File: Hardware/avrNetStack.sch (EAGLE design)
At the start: 36 parts, among them IC1 MEGA48/88/168-PU, IC2 ENC28J60SP, Q1 16M, Q2 25M

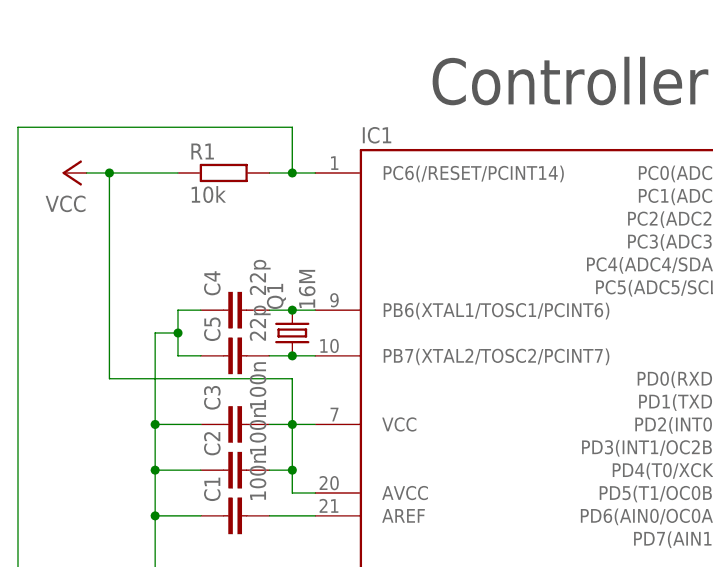
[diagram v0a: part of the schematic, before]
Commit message: AVR runs with 20MHz
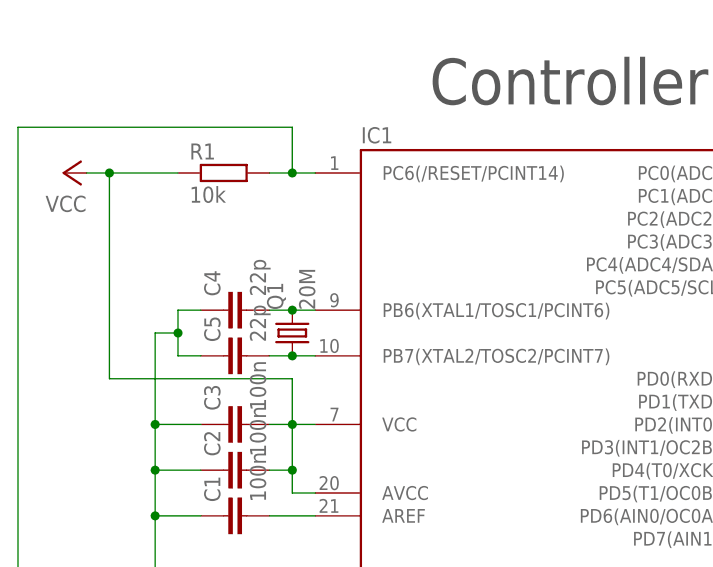
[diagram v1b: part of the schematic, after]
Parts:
- Q1: value 16M -> 20M
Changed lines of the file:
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@@
 <part name="C4" library="resistor" deviceset="C-EU" device="025-030X050" value="22p"/>
 <part name="C5" library="resistor" deviceset="C-EU" device="025-030X050" value="22p"/>
-<part name="Q1" library="crystal" deviceset="CRYSTAL" device="HC49S" value="16M"/>
+<part name="Q1" library="crystal" deviceset="CRYSTAL" device="HC49S" value="20M"/>
 <part name="JP1" library="0_RN" deviceset="AVR-ISP" device=""/>
 <part name="GND2" library="supply1" deviceset="GND" device=""/>

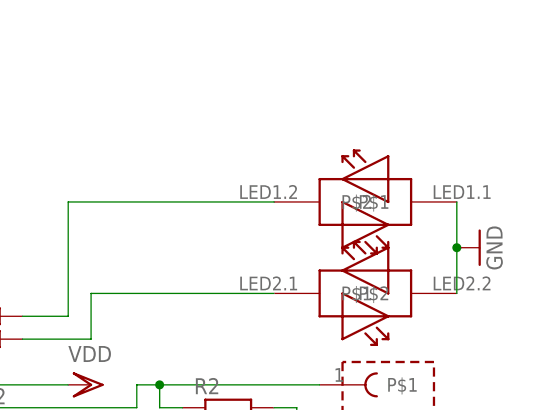
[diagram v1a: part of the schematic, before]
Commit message: Added PHY Initialization for ENC
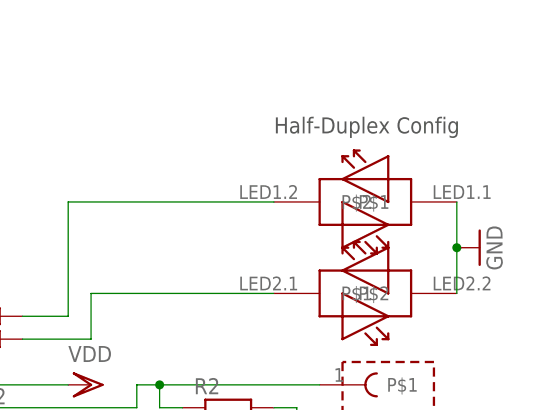
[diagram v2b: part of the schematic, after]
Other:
- note added: "Half-Duplex Config"
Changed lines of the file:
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@@
 <text x="177.8" y="109.22" size="1.27" layer="97">AVR Input is 3V3 tolerant</text>
 <text x="175.26" y="111.76" size="1.27" layer="97">ENC &amp; MRF Input is 5V5 Tolerant</text>
+<text x="332.74" y="109.22" size="1.778" layer="97">Half-Duplex Config</text>
 </plain>
 <instances>

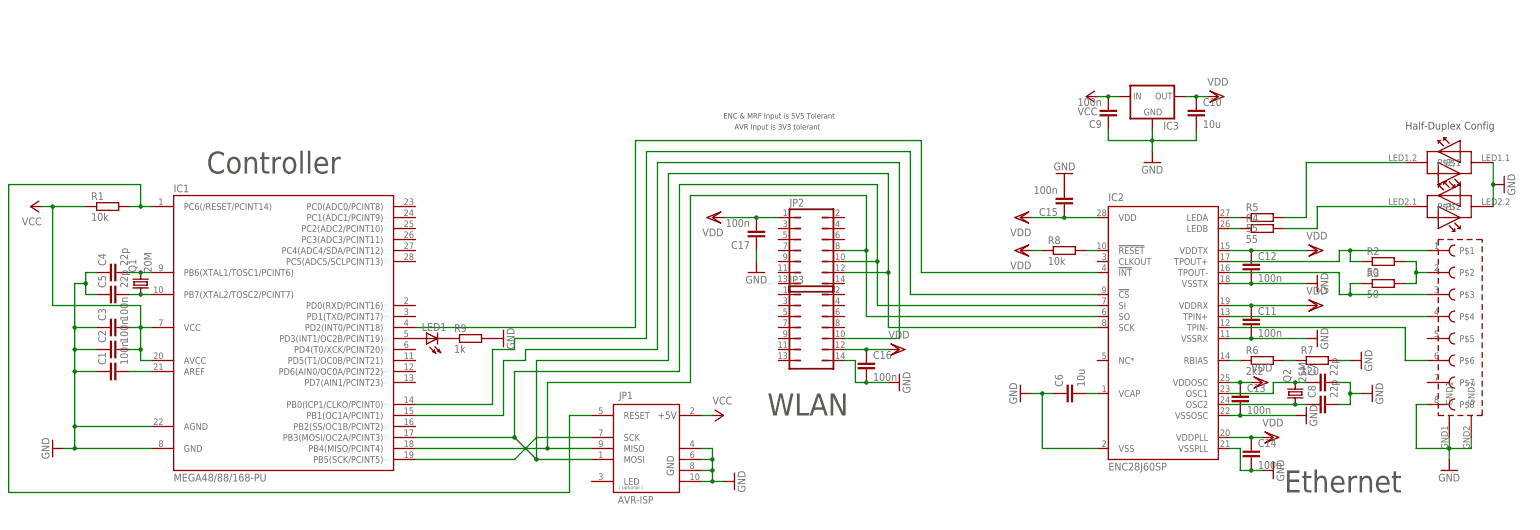
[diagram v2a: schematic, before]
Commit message: Changed Schematic for AtMega32.
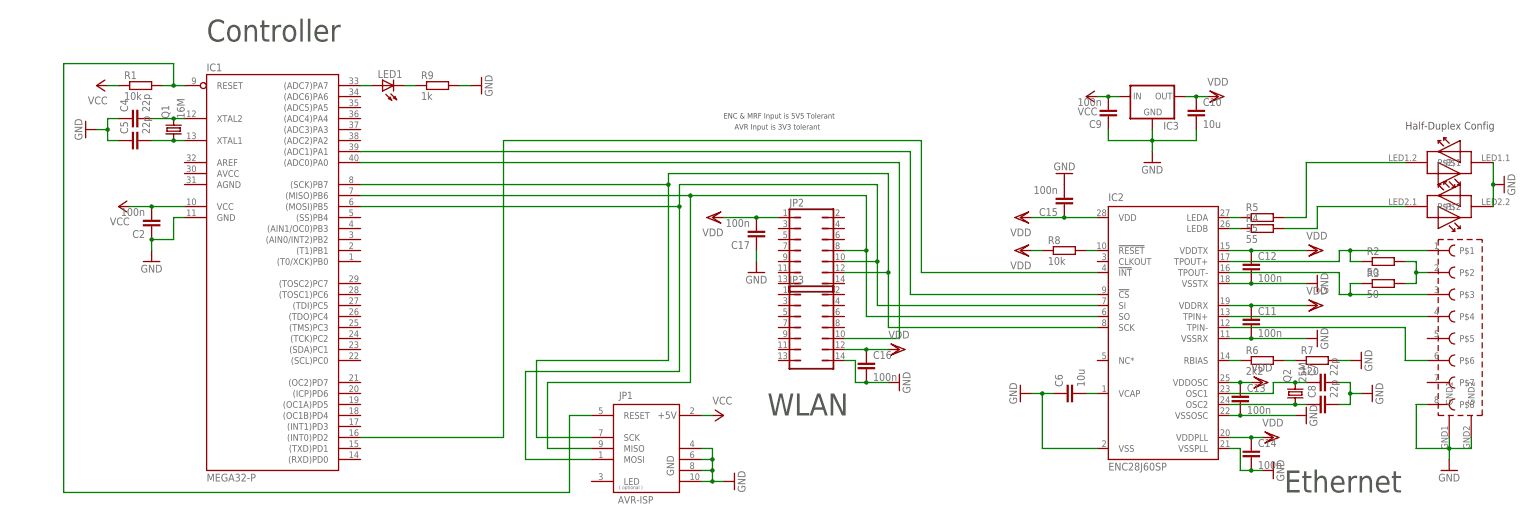
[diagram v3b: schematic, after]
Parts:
- removed C1, C3: 100n, resistor:C-EU025-030X050
- IC1: value MEGA48/88/168-PU -> MEGA32-P; device avr-7:MEGA48/88/168-PU -> avr-7:MEGA32-P
- Q1: value 20M -> 16M
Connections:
- removed net N$9: IC1.PB5(SCK/PCINT5), JP1.SCK
- net GND: now also IC1.GND; no longer C1.1, C3.1, IC1.AGND, IC1.GND@1
- net N$1: now also IC1.RESET; no longer IC1.PC6(/RESET/PCINT14)
- net N$12: now also IC1.(ADC0)PA0; no longer IC1.PB1(OC1A/PCINT1)
- net N$13: now also IC1.(ADC1)PA1; no longer IC1.PB0(ICP1/CLKO/PCINT0)
- net N$14: now also IC1.(SCK)PB7, IC2.SCK, JP1.SCK, JP2.12; no longer IC1.PD2(INT0/PCINT18), IC2.!INT
- net N$18: now also IC1.(ADC7)PA7; no longer IC1.PD3(INT1/OC2B/PCINT19)
- net N$2: now also IC1.(INT0)PD2, IC2.!INT; no longer C1.2, IC1.AREF
- net N$4: now also IC1.(MISO)PB6; no longer IC1.PB4(MISO/PCINT4)
- net N$5: now also IC1.XTAL1; no longer IC1.PB7(XTAL2/TOSC2/PCINT7)
- net N$6: now also IC1.XTAL2; no longer IC1.PB6(XTAL1/TOSC1/PCINT6)
- net N$7: now also IC1.(MOSI)PB5; no longer IC1.PB3(MOSI/OC2A/PCINT3), IC2.SCK, JP2.12
- net VCC: now also IC1.VCC; no longer C3.2, IC1.AVCC, IC1.VCC@1
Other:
- moved on the sheet: C2, C4, C5, LED1, Q1, R1, R9

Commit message: Built Test Hardware.
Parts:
- added JP4: AVR_JTAG, 0_RN:AVR_JTAG
- added LED2: (no value), led:LED5MM
- added R10: 1k, resistor:R-EU_0204/7
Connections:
- new net N$28: LED2.C, R10.1
- new net N$29: IC1.(TDI)PC5, JP4.TDI
- new net N$30: IC1.(TMS)PC3, JP4.TMS
- new net N$31: IC1.(TDO)PC4, JP4.TDO
- new net N$32: IC1.(TCK)PC2, JP4.TCK
- new net N$9: IC1.(ADC6)PA6, LED2.A
- net GND: now also JP4.GND, JP4.GND@1, R10.2
- net N$1: now also JP4.NSRST
- net VCC: now also JP4.VCC, JP4.VREF
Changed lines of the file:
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@@
 <part name="P+4" library="supply1" deviceset="VCC" device=""/>
 <part name="GND17" library="supply1" deviceset="GND" device=""/>
+<part name="LED2" library="led" deviceset="LED" device="5MM"/>
+<part name="R10" library="resistor" deviceset="R-EU_" device="0204/7" value="1k"/>
+<part name="JP4" library="0_RN" deviceset="AVR_JTAG" device=""/>
+<part name="P+5" library="supply1" deviceset="VCC" device=""/>
+<part name="GND18" library="supply1" deviceset="GND" device=""/>
 </parts>
 <sheets>
@@
 <instance part="LED1" gate="G$1" x="96.52" y="119.38" rot="R90"/>
 <instance part="R9" gate="G$1" x="109.22" y="119.38"/>
-<instance part="GND13" gate="1" x="119.38" y="119.38" rot="R90"/>
+<instance part="GND13" gate="1" x="121.92" y="119.38" rot="R90"/>
 <instance part="IC3" gate="1" x="274.32" y="116.84"/>
 <instance part="C9" gate="G$1" x="264.16" y="111.76" rot="R180"/>
@@
 <instance part="P+4" gate="VCC" x="35.56" y="91.44" rot="R90"/>
 <instance part="GND17" gate="1" x="27.94" y="109.22" rot="R270"/>
+<instance part="LED2" gate="G$1" x="96.52" y="116.84" rot="R90"/>
+<instance part="R10" gate="G$1" x="109.22" y="116.84"/>
+<instance part="JP4" gate="JP" x="142.24" y="71.12"/>
+<instance part="P+5" gate="VCC" x="154.94" y="83.82"/>
+<instance part="GND18" gate="1" x="160.02" y="63.5" rot="R90"/>
 </instances>
 <busses>
@@
 <wire x1="144.78" y1="43.18" x2="139.7" y2="43.18" width="0.1524" layer="91"/>
 <wire x1="139.7" y1="43.18" x2="139.7" y2="25.4" width="0.1524" layer="91"/>
-<wire x1="139.7" y1="25.4" x2="22.86" y2="25.4" width="0.1524" layer="91"/>
+<wire x1="139.7" y1="25.4" x2="127" y2="25.4" width="0.1524" layer="91"/>
+<wire x1="127" y1="25.4" x2="22.86" y2="25.4" width="0.1524" layer="91"/>
 <wire x1="22.86" y1="25.4" x2="22.86" y2="124.46" width="0.1524" layer="91"/>
 <pinref part="IC1" gate="G$1" pin="RESET"/>
@@
 <wire x1="48.26" y1="124.46" x2="48.26" y2="119.38" width="0.1524" layer="91"/>
 <junction x="48.26" y="119.38"/>
+<pinref part="JP4" gate="JP" pin="NSRST"/>
+<wire x1="129.54" y1="78.74" x2="127" y2="78.74" width="0.1524" layer="91"/>
+<wire x1="127" y1="78.74" x2="127" y2="25.4" width="0.1524" layer="91"/>
+<junction x="127" y="25.4"/>
 </segment>
 </net>
@@
 <pinref part="P+1" gate="VCC" pin="VCC"/>
 <wire x1="35.56" y1="119.38" x2="33.02" y2="119.38" width="0.1524" layer="91"/>
+</segment>
+<segment>
+<pinref part="JP4" gate="JP" pin="VREF"/>
+<wire x1="152.4" y1="71.12" x2="154.94" y2="71.12" width="0.1524" layer="91"/>
+<wire x1="154.94" y1="71.12" x2="154.94" y2="78.74" width="0.1524" layer="91"/>
+<pinref part="JP4" gate="JP" pin="VCC"/>
+<wire x1="154.94" y1="78.74" x2="152.4" y2="78.74" width="0.1524" layer="91"/>
+<pinref part="P+5" gate="VCC" pin="VCC"/>
+<wire x1="154.94" y1="78.74" x2="154.94" y2="81.28" width="0.1524" layer="91"/>
+<junction x="154.94" y="78.74"/>
 </segment>
 </net>
@@
 <pinref part="GND13" gate="1" pin="GND"/>
 <wire x1="114.3" y1="119.38" x2="116.84" y2="119.38" width="0.1524" layer="91"/>
+<pinref part="R10" gate="G$1" pin="2"/>
+<wire x1="116.84" y1="119.38" x2="119.38" y2="119.38" width="0.1524" layer="91"/>
+<wire x1="114.3" y1="116.84" x2="116.84" y2="116.84" width="0.1524" layer="91"/>
+<wire x1="116.84" y1="116.84" x2="116.84" y2="119.38" width="0.1524" layer="91"/>
+<junction x="116.84" y="119.38"/>
 </segment>
 <segment>
@@
 <wire x1="33.02" y1="106.68" x2="33.02" y2="109.22" width="0.1524" layer="91"/>
 <junction x="33.02" y="109.22"/>
+</segment>
+<segment>
+<pinref part="GND18" gate="1" pin="GND"/>
+<wire x1="157.48" y1="63.5" x2="154.94" y2="63.5" width="0.1524" layer="91"/>
+<wire x1="154.94" y1="63.5" x2="154.94" y2="66.04" width="0.1524" layer="91"/>
+<pinref part="JP4" gate="JP" pin="GND"/>
+<wire x1="154.94" y1="66.04" x2="152.4" y2="66.04" width="0.1524" layer="91"/>
+<pinref part="JP4" gate="JP" pin="GND@1"/>
+<wire x1="152.4" y1="63.5" x2="154.94" y2="63.5" width="0.1524" layer="91"/>
+<junction x="154.94" y="63.5"/>
 </segment>
 </net>
@@
 </segment>
 </net>
+<net name="N$9" class="0">
+<segment>
+<pinref part="IC1" gate="G$1" pin="(ADC6)PA6"/>
+<pinref part="LED2" gate="G$1" pin="A"/>
+<wire x1="91.44" y1="116.84" x2="93.98" y2="116.84" width="0.1524" layer="91"/>
+</segment>
+</net>
+<net name="N$28" class="0">
+<segment>
+<pinref part="LED2" gate="G$1" pin="C"/>
+<pinref part="R10" gate="G$1" pin="1"/>
+<wire x1="101.6" y1="116.84" x2="104.14" y2="116.84" width="0.1524" layer="91"/>
+</segment>
+</net>
+<net name="N$29" class="0">
+<segment>
+<pinref part="IC1" gate="G$1" pin="(TDI)PC5"/>
+<wire x1="91.44" y1="68.58" x2="114.3" y2="68.58" width="0.1524" layer="91"/>
+<wire x1="114.3" y1="68.58" x2="114.3" y2="63.5" width="0.1524" layer="91"/>
+<pinref part="JP4" gate="JP" pin="TDI"/>
+<wire x1="114.3" y1="63.5" x2="129.54" y2="63.5" width="0.1524" layer="91"/>
+</segment>
+</net>
+<net name="N$30" class="0">
+<segment>
+<pinref part="JP4" gate="JP" pin="TMS"/>
+<wire x1="129.54" y1="66.04" x2="111.76" y2="66.04" width="0.1524" layer="91"/>
+<wire x1="111.76" y1="66.04" x2="111.76" y2="63.5" width="0.1524" layer="91"/>
+<pinref part="IC1" gate="G$1" pin="(TMS)PC3"/>
+<wire x1="111.76" y1="63.5" x2="91.44" y2="63.5" width="0.1524" layer="91"/>
+</segment>
+</net>
+<net name="N$31" class="0">
+<segment>
+<pinref part="IC1" gate="G$1" pin="(TDO)PC4"/>
+<wire x1="91.44" y1="66.04" x2="109.22" y2="66.04" width="0.1524" layer="91"/>
+<wire x1="109.22" y1="66.04" x2="109.22" y2="71.12" width="0.1524" layer="91"/>
+<wire x1="109.22" y1="71.12" x2="116.84" y2="71.12" width="0.1524" layer="91"/>
+<wire x1="116.84" y1="71.12" x2="116.84" y2="68.58" width="0.1524" layer="91"/>
+<pinref part="JP4" gate="JP" pin="TDO"/>
+<wire x1="116.84" y1="68.58" x2="129.54" y2="68.58" width="0.1524" layer="91"/>
+</segment>
+</net>
+<net name="N$32" class="0">
+<segment>
+<pinref part="JP4" gate="JP" pin="TCK"/>
+<wire x1="129.54" y1="71.12" x2="119.38" y2="71.12" width="0.1524" layer="91"/>
+<wire x1="119.38" y1="71.12" x2="119.38" y2="60.96" width="0.1524" layer="91"/>
+<pinref part="IC1" gate="G$1" pin="(TCK)PC2"/>
+<wire x1="119.38" y1="60.96" x2="91.44" y2="60.96" width="0.1524" layer="91"/>
+</segment>
+</net>

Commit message: Extended capabilities.
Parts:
- added L1: (no value), resistor:L-EU0204/7
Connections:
- net N$16: now also L1.1
- net VDD: now also L1.2
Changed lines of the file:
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@@
 <part name="P+5" library="supply1" deviceset="VCC" device=""/>
 <part name="GND18" library="supply1" deviceset="GND" device=""/>
+<part name="L1" library="resistor" deviceset="L-EU" device="0204/7"/>
+<part name="VDD10" library="supply1" deviceset="VDD" device=""/>
 </parts>
 <sheets>
@@
 <instance part="R2" gate="G$1" x="327.66" y="78.74"/>
 <instance part="R3" gate="G$1" x="327.66" y="73.66"/>
-<instance part="U$1" gate="G$1" x="345.44" y="66.04"/>
+<instance part="U$1" gate="G$1" x="350.52" y="66.04"/>
 <instance part="U$1" gate="G$2" x="342.9" y="104.14" rot="R180"/>
 <instance part="U$1" gate="G$3" x="342.9" y="88.9"/>
-<instance part="GND5" gate="1" x="342.9" y="30.48"/>
+<instance part="GND5" gate="1" x="347.98" y="30.48"/>
 <instance part="R4" gate="G$1" x="299.72" y="86.36"/>
 <instance part="R5" gate="G$1" x="299.72" y="88.9"/>
@@
 <instance part="P+5" gate="VCC" x="154.94" y="83.82"/>
 <instance part="GND18" gate="1" x="160.02" y="63.5" rot="R90"/>
+<instance part="L1" gate="G$1" x="337.82" y="68.58"/>
+<instance part="VDD10" gate="G$1" x="337.82" y="58.42" rot="R180"/>
 </instances>
 <busses>
@@
 <pinref part="GND5" gate="1" pin="GND"/>
 <pinref part="U$1" gate="G$1" pin="GND1"/>
-<wire x1="342.9" y1="33.02" x2="342.9" y2="35.56" width="0.1524" layer="91"/>
+<wire x1="347.98" y1="33.02" x2="347.98" y2="35.56" width="0.1524" layer="91"/>
 <pinref part="U$1" gate="G$1" pin="GND2"/>
-<wire x1="342.9" y1="35.56" x2="342.9" y2="38.1" width="0.1524" layer="91"/>
-<wire x1="342.9" y1="35.56" x2="347.98" y2="35.56" width="0.1524" layer="91"/>
 <wire x1="347.98" y1="35.56" x2="347.98" y2="38.1" width="0.1524" layer="91"/>
-<junction x="342.9" y="35.56"/>
+<wire x1="347.98" y1="35.56" x2="353.06" y2="35.56" width="0.1524" layer="91"/>
+<wire x1="353.06" y1="35.56" x2="353.06" y2="38.1" width="0.1524" layer="91"/>
+<junction x="347.98" y="35.56"/>
 <pinref part="U$1" gate="G$1" pin="P$8"/>
-<wire x1="337.82" y1="45.72" x2="335.28" y2="45.72" width="0.1524" layer="91"/>
-<wire x1="335.28" y1="45.72" x2="335.28" y2="35.56" width="0.1524" layer="91"/>
-<wire x1="335.28" y1="35.56" x2="342.9" y2="35.56" width="0.1524" layer="91"/>
+<wire x1="342.9" y1="45.72" x2="340.36" y2="45.72" width="0.1524" layer="91"/>
+<wire x1="340.36" y1="45.72" x2="340.36" y2="35.56" width="0.1524" layer="91"/>
+<wire x1="340.36" y1="35.56" x2="347.98" y2="35.56" width="0.1524" layer="91"/>
 </segment>
 <segment>
@@
 <wire x1="317.5" y1="81.28" x2="320.04" y2="81.28" width="0.1524" layer="91"/>
 <pinref part="R2" gate="G$1" pin="1"/>
-<wire x1="320.04" y1="81.28" x2="337.82" y2="81.28" width="0.1524" layer="91"/>
+<wire x1="320.04" y1="81.28" x2="342.9" y2="81.28" width="0.1524" layer="91"/>
 <wire x1="322.58" y1="78.74" x2="320.04" y2="78.74" width="0.1524" layer="91"/>
 <wire x1="320.04" y1="78.74" x2="320.04" y2="81.28" width="0.1524" layer="91"/>
@@
 <net name="N$10" class="0">
 <segment>
-<wire x1="337.82" y1="71.12" x2="320.04" y2="71.12" width="0.1524" layer="91"/>
+<wire x1="342.9" y1="71.12" x2="320.04" y2="71.12" width="0.1524" layer="91"/>
 <wire x1="320.04" y1="71.12" x2="317.5" y2="71.12" width="0.1524" layer="91"/>
 <wire x1="317.5" y1="71.12" x2="317.5" y2="76.2" width="0.1524" layer="91"/>
@@
 <segment>
 <pinref part="IC2" gate="G$1" pin="TPIN+"/>
-<wire x1="292.1" y1="66.04" x2="337.82" y2="66.04" width="0.1524" layer="91"/>
+<wire x1="292.1" y1="66.04" x2="342.9" y2="66.04" width="0.1524" layer="91"/>
 <pinref part="U$1" gate="G$1" pin="P$4"/>
 </segment>
@@
 <wire x1="335.28" y1="76.2" x2="337.82" y2="76.2" width="0.1524" layer="91"/>
 <pinref part="R3" gate="G$1" pin="2"/>
+<wire x1="337.82" y1="76.2" x2="342.9" y2="76.2" width="0.1524" layer="91"/>
 <wire x1="332.74" y1="73.66" x2="335.28" y2="73.66" width="0.1524" layer="91"/>
 <wire x1="335.28" y1="73.66" x2="335.28" y2="76.2" width="0.1524" layer="91"/>
 <junction x="335.28" y="76.2"/>
 <pinref part="U$1" gate="G$1" pin="P$2"/>
+<pinref part="L1" gate="G$1" pin="1"/>
+<wire x1="337.82" y1="73.66" x2="337.82" y2="76.2" width="0.1524" layer="91"/>
+<junction x="337.82" y="76.2"/>
 </segment>
 </net>
 <net name="N$17" class="0">
 <segment>
-<wire x1="337.82" y1="55.88" x2="332.74" y2="55.88" width="0.1524" layer="91"/>
+<wire x1="342.9" y1="55.88" x2="332.74" y2="55.88" width="0.1524" layer="91"/>
 <wire x1="332.74" y1="55.88" x2="332.74" y2="63.5" width="0.1524" layer="91"/>
 <pinref part="IC2" gate="G$1" pin="TPIN-"/>
@@
 <junction x="208.28" y="58.42"/>
 </segment>
-</net>
+<segment>
+<pinref part="VDD10" gate="G$1" pin="VDD"/>
+<pinref part="L1" gate="G$1" pin="2"/>
+<wire x1="337.82" y1="60.96" x2="337.82" y2="63.5" width="0.1524" layer="91"/>
+</segment>
+</net>

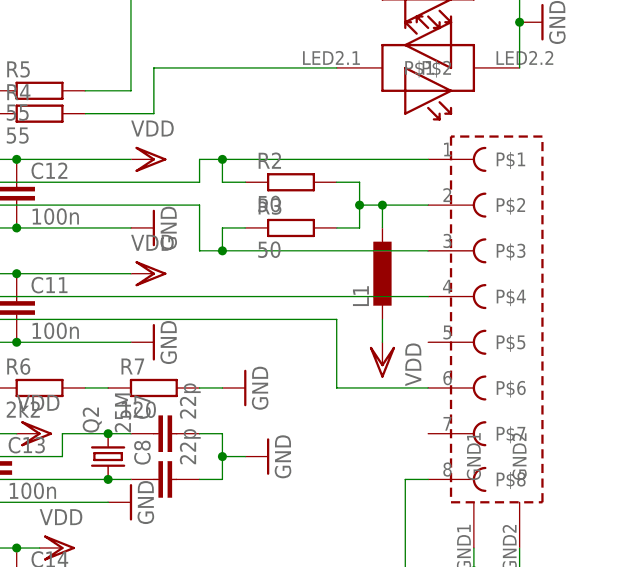
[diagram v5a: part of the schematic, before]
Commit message: Fixed Hardware Bug.
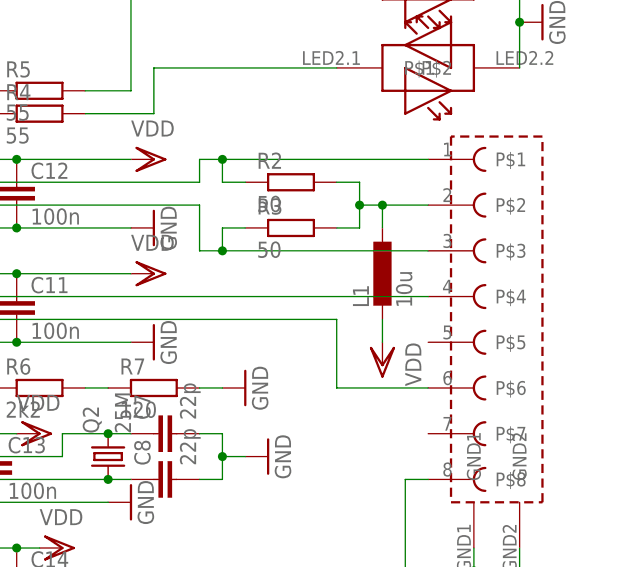
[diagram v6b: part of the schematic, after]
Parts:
- L1: value (none) -> 10u
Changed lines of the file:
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@@
 <part name="P+5" library="supply1" deviceset="VCC" device=""/>
 <part name="GND18" library="supply1" deviceset="GND" device=""/>
-<part name="L1" library="resistor" deviceset="L-EU" device="0204/7"/>
+<part name="L1" library="resistor" deviceset="L-EU" device="0204/7" value="10u"/>
 <part name="VDD10" library="supply1" deviceset="VDD" device=""/>
 </parts>
